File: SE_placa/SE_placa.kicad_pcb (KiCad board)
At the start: 2 copper layers, 118.1 x 58.4 mm, 70 parts, among them IC1 TP4056, J1 5V, J2 Micro_SD_Card_Det_Hirose_DM3AT, J3 Conn_02x07_ESP32_IO, J4 I2C-0, J5 I2C-1, J6 Conn_02x03_LORA_IO, J7 U.FL-R-SMT(01), J8 UART, J9 Connector Bateria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

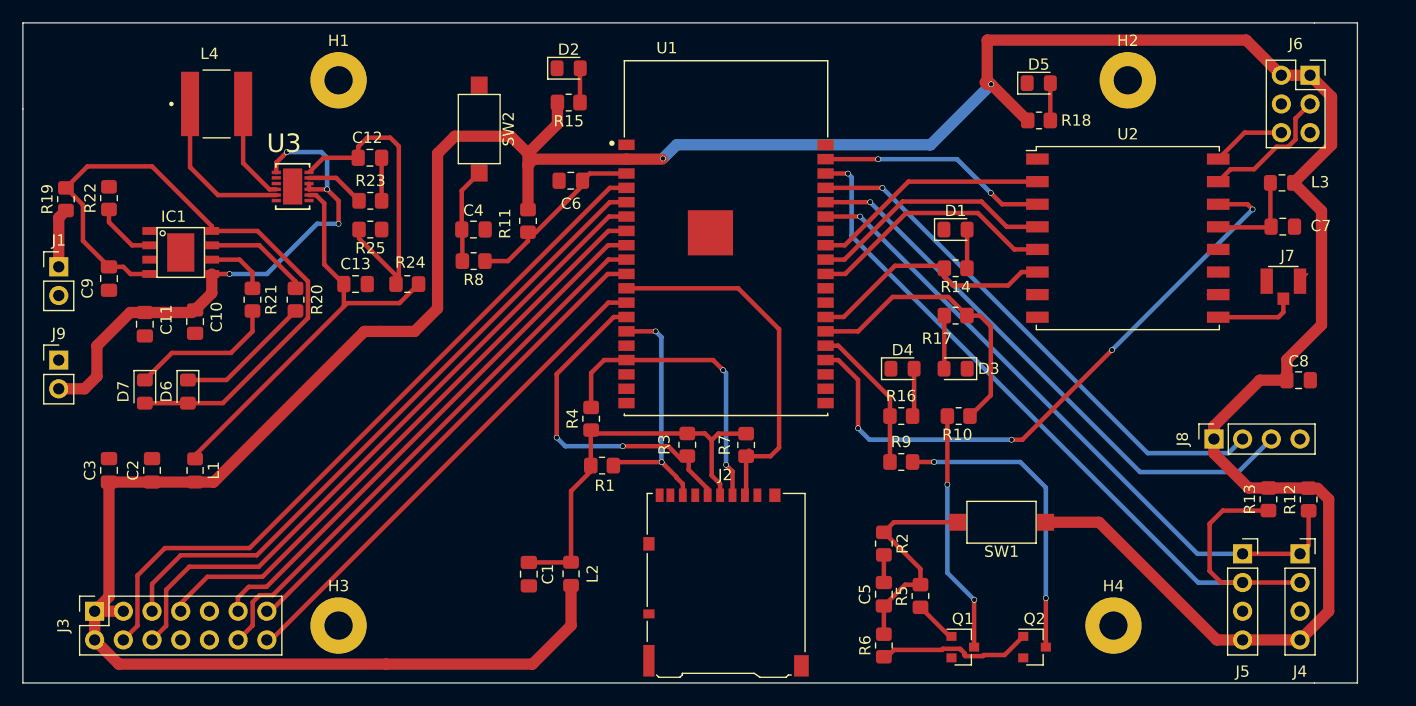
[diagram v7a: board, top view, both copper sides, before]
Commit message: Ruteo 3
1. Cambio orden de los pines de I/O para hacer mas facil el ruteo de los conectores, modifico ubicacion de I/Os del Lora
2. Cambio huella del LTC 3441 al parecer la que tenia creaba conflictos con las rutas y sus anchos
3. cambio el esquema de Net classes a default, arreglando el tamaño de las rutas y de las vias .
4. Modifico la ruta a 0.3 mm , agrego esto a pre definidas
5. agrego ruta de 1 mm y vias de 1.8 mm para alimentaciones
6. cambio ubicaciones de conectorres de bateria y de panel solar
7. cambio ubicacion del TP4056 y modifico la ubicacion de los componentes cercanos.
8. Falta agregar plano de tierra en las dos caras y modificar salida de potencia de la entrada y la salida del LTC 3441
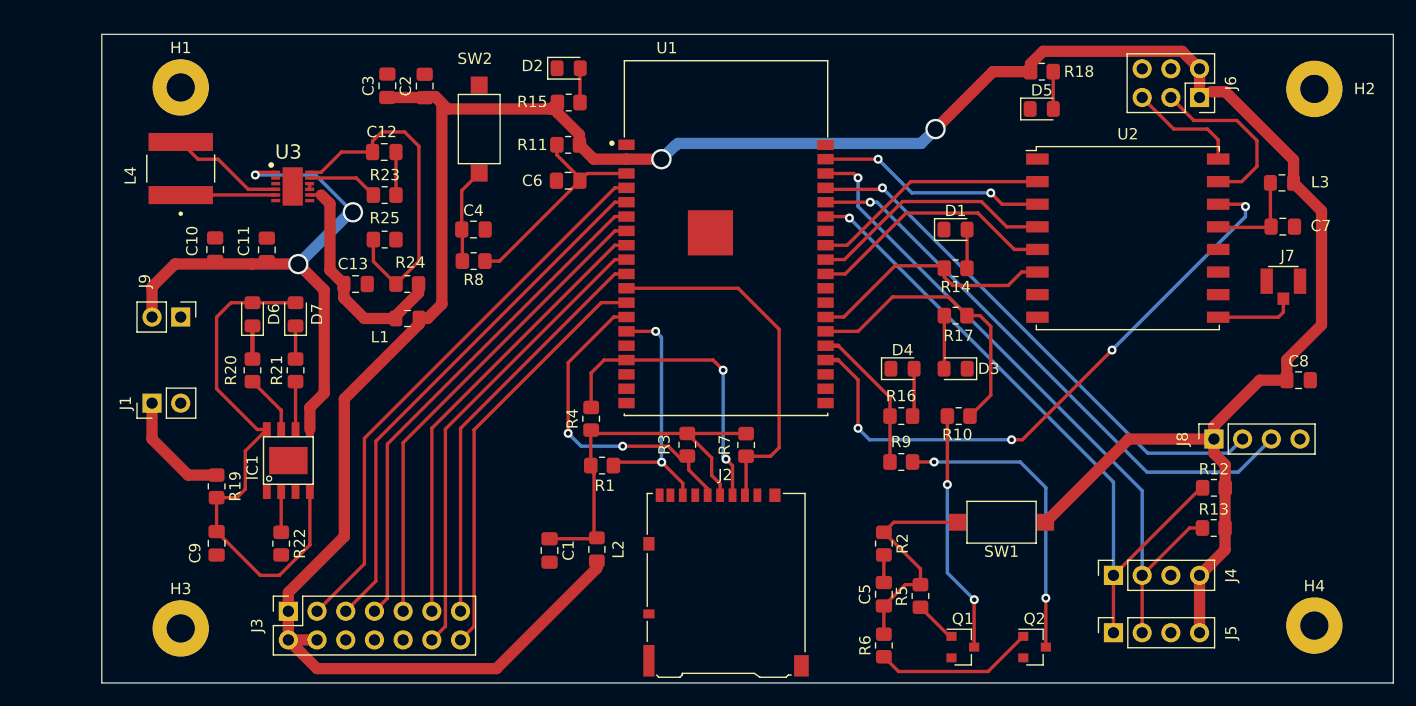
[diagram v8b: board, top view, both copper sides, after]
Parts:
- U3: footprint LTC3441EDEPBF:DFN400X300X80-13N -> LTC3441EDE#PBF:SON50P300X400X80-13N-D
- moved C3 42.0 mm to (133.9, 23.3)
- moved C2 41.7 mm to (137.2, 23.4)
- moved R22 34.2 mm to (124.5, 63.9), turned to 270 degrees
- moved R19 28.7 mm to (118.7, 58.8), turned to 270 degrees
- moved C9 25.3 mm to (118.7, 63.8)
- moved L1 23.1 mm to (135.6, 43.9), turned to 0 degrees
- moved IC1 20.7 mm to (125.1, 56.5), turned to 90 degrees
- moved H4 17.8 mm to (215.9, 71.1)
- moved J3 17.1 mm to (125.1, 69.8)
- moved J4 16.6 mm to (198.1, 66.7), turned to 90 degrees
- moved H2 16.5 mm to (215.9, 23.6)
- moved D7 15.0 mm to (125.7, 43.6), turned to 90 degrees
- moved J1 14.6 mm to (113.0, 51.4), turned to 90 degrees
- moved H1 14.0 mm to (115.6, 23.5)
- moved H3 14.0 mm to (115.6, 71.4)
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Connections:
- J3 pad 3: +3V3 -> /I36
- J3 pad 4: /I36 -> +3V3
- J3 pad 6: /I34 -> GND
- J3 pad 7: /I35 -> /I34
- J3 pad 9: GND -> /I35
- J6 pad 5: GND -> /L-DIO2
- J6 pad 6: /L-DIO2 -> GND
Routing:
- net +3V3: track 311.9 -> 250.1 mm
- net /cargador_regulador/Vout3.3V: track 37.9 -> 20.2 mm
- net /I34: track 59.4 -> 44.8 mm
- net /I36: track 63.7 -> 49.4 mm
- net Net-(C9-Pad1): track 60.3 -> 47.4 mm
- net /I2C-SCL: track 73.3 -> 60.8 mm
- net /I35: track 53.8 -> 42.4 mm
- net /I39: track 58.4 -> 47.1 mm
- net Net-(D7-Pad1): track 13.6 -> 3.39 mm
- net Net-(D6-Pad1): track 12.1 -> 2.94 mm
- net /IO32: track 48.5 -> 40.1 mm
- net /IO33: track 49.5 -> 41.4 mm
- net /IO25: track 44.2 -> 36.5 mm
- net /IO12: track 44.2 -> 37.2 mm
- net Net-(L4-Pad1): track 14.2 -> 8.78 mm
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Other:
- board size 118.1 x 58.4 mm -> 114.3 x 57.4 mm
- net class Default: trace_width 0.4 -> 0.25; via_dia 0.5 -> 0.8
- rule trace_min: 0.4 -> 0.2
